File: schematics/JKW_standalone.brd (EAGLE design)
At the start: 159.4 x 80.7 mm, 241 parts, among them IC1 4093D, IC4 ATMEGA2560-16AU, Q1 BSS84, Q10 BSS84, Q11 BSS84, Q2 BSS84, Q3 BSS84, Q4 BSS84, Q5 BSS84, Q6 BSS84, Q7 BSS84, Q8 BSS84, Q9 BSS84, T1 Mouser: 771-2N7002BK215 , N-C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, T10 Mouser: 771-2N7002BK215 , N-C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, T11 Mouser: 771-2N7002BK215 , N-C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, T12 Mouser: 771-2N7002BK215 , N-C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, T13 Mouser: 771-2N7002BK215 , N-C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, T2 Mouser: 771-2N7002BK215 , N-C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, T3 Mouser: 771-2N7002BK215 , N-C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, T5 Mouser: 771-2N7002BK215 , N-C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, T6 Mouser: 771-2N7002BK215 , N-C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, T7 Mouser: 771-2N7002BK215 , N-C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, T8 Mouser: 771-2N7002BK215 , N-C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, T9 Mouser: 771-2N7002BK215 , N-C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

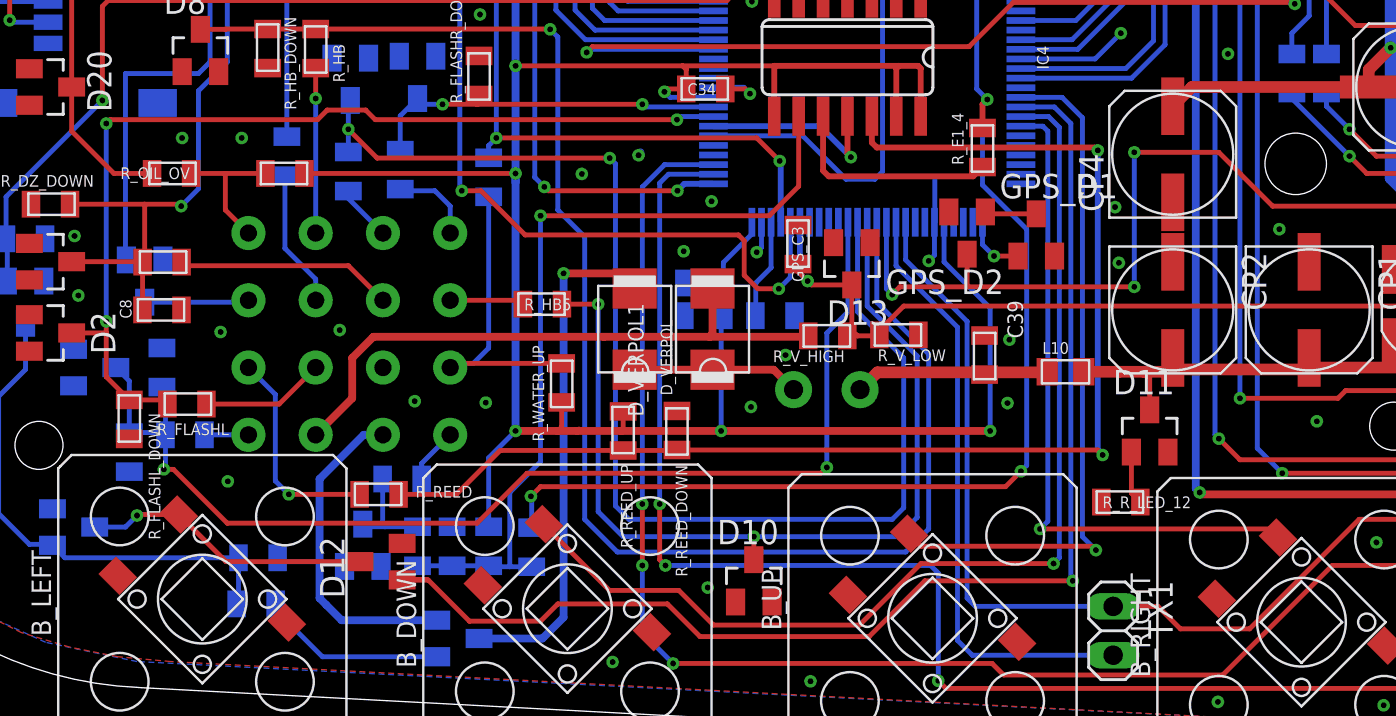
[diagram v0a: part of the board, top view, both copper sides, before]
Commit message: Readded Taster, changed pinning of taster, reduced resistor value, removed bat measurement connection (broke)
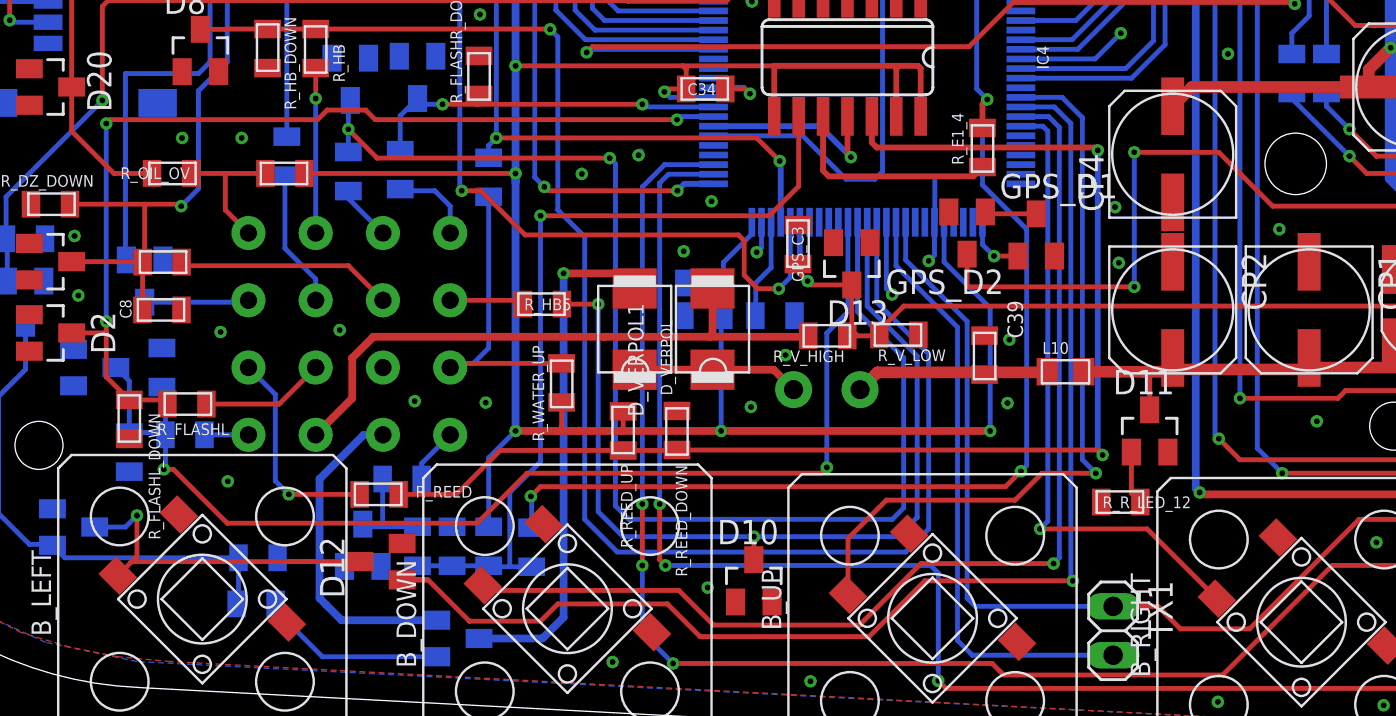
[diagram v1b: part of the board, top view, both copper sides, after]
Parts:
- R_L3: value 1k -> 10k
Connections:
- new net V_BAT: D15.C, GPS.VBACKUP, GPS_C2.1, GPS_D2.3
- net A11: no longer D15.C, GPS.VBACKUP, GPS_C2.1, GPS_D2.3
- net B_DOWN: now also B_DOWN.OUT; no longer B_DOWN.OUT1
- net B_LEFT: now also B_LEFT.OUT; no longer B_LEFT.OUT1
- net B_RIGHT: now also B_RIGHT.OUT; no longer B_RIGHT.OUT1
- net B_UP: now also B_UP.OUT; no longer B_UP.OUT1
- net GND: now also B_DOWN.IN2, B_LEFT.IN2, B_RIGHT.IN2, B_UP.IN2
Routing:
- net A11: track 111.8 -> 3.88 mm, vias 7 -> 1
- net V_BAT: track 0.00 -> 103.9 mm, vias 0 -> 6
- net B_UP: track 36.5 -> 39.7 mm
- net B_LEFT: track 15.1 -> 17.9 mm
- net B_RIGHT: track 35.0 -> 33.1 mm
- net B_DOWN: track 55.1 -> 56.9 mm

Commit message: Changed value of pullup to 15k
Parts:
- R_REED_DOWN: value 5k / n.b. (Reed / 5V Honda Signal) -> 5k / n.b. (12V Signal / 5V Signal)
- R_REED_UP: value n.b.(Honda Signal) / 5k (Reed) -> n.b.(Honda Signal) / 15k (Reed)
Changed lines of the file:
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@@
 <?xml version="1.0" encoding="utf-8"?>
 <!DOCTYPE eagle SYSTEM "eagle.dtd">
-<eagle version="6.2">
+<eagle version="6.4">
 <drawing>
 <settings>
@@
 </class>
 </classes>
-<designrules>
+<designrules name="default">
 <description language="de">DRC von Lutz
 Via´s bis 0.6mm mit Lötstoplack überzogen
@@
 <attribute name="NAME" x="133.1325" y="50.9975" size="0.6096" layer="26" rot="MR90"/>
 </element>
-<element name="R_REED_DOWN" library="RCLDT" package="0805" value="5k / n.b. (Reed / 5V Honda Signal)" x="38.6" y="17.525" smashed="yes" rot="R90">
+<element name="R_REED_DOWN" library="RCLDT" package="0805" value="5k / n.b. (12V Signal / 5V Signal)" x="38.6" y="17.525" smashed="yes" rot="R90">
 <attribute name="NAME" x="38.5325" y="15.7275" size="0.6096" layer="25" rot="R270"/>
 </element>
@@
 </element>
 <element name="D8" library="diode" package="SOT23" value="5.5V" x="13.8" y="37.3"/>
-<element name="R_REED_UP" library="RCLDT" package="0805" value="n.b.(Honda Signal) / 5k (Reed)" x="35.8" y="17.5" smashed="yes" rot="R270">
+<element name="R_REED_UP" library="RCLDT" package="0805" value="n.b.(Honda Signal) / 15k (Reed)" x="35.8" y="17.5" smashed="yes" rot="R270">
 <attribute name="NAME" x="35.6825" y="15.7525" size="0.6096" layer="25" rot="R270"/>
 <attribute name="VALUE" x="34.1825" y="20.1525" size="0.6096" layer="27" rot="R270"/>

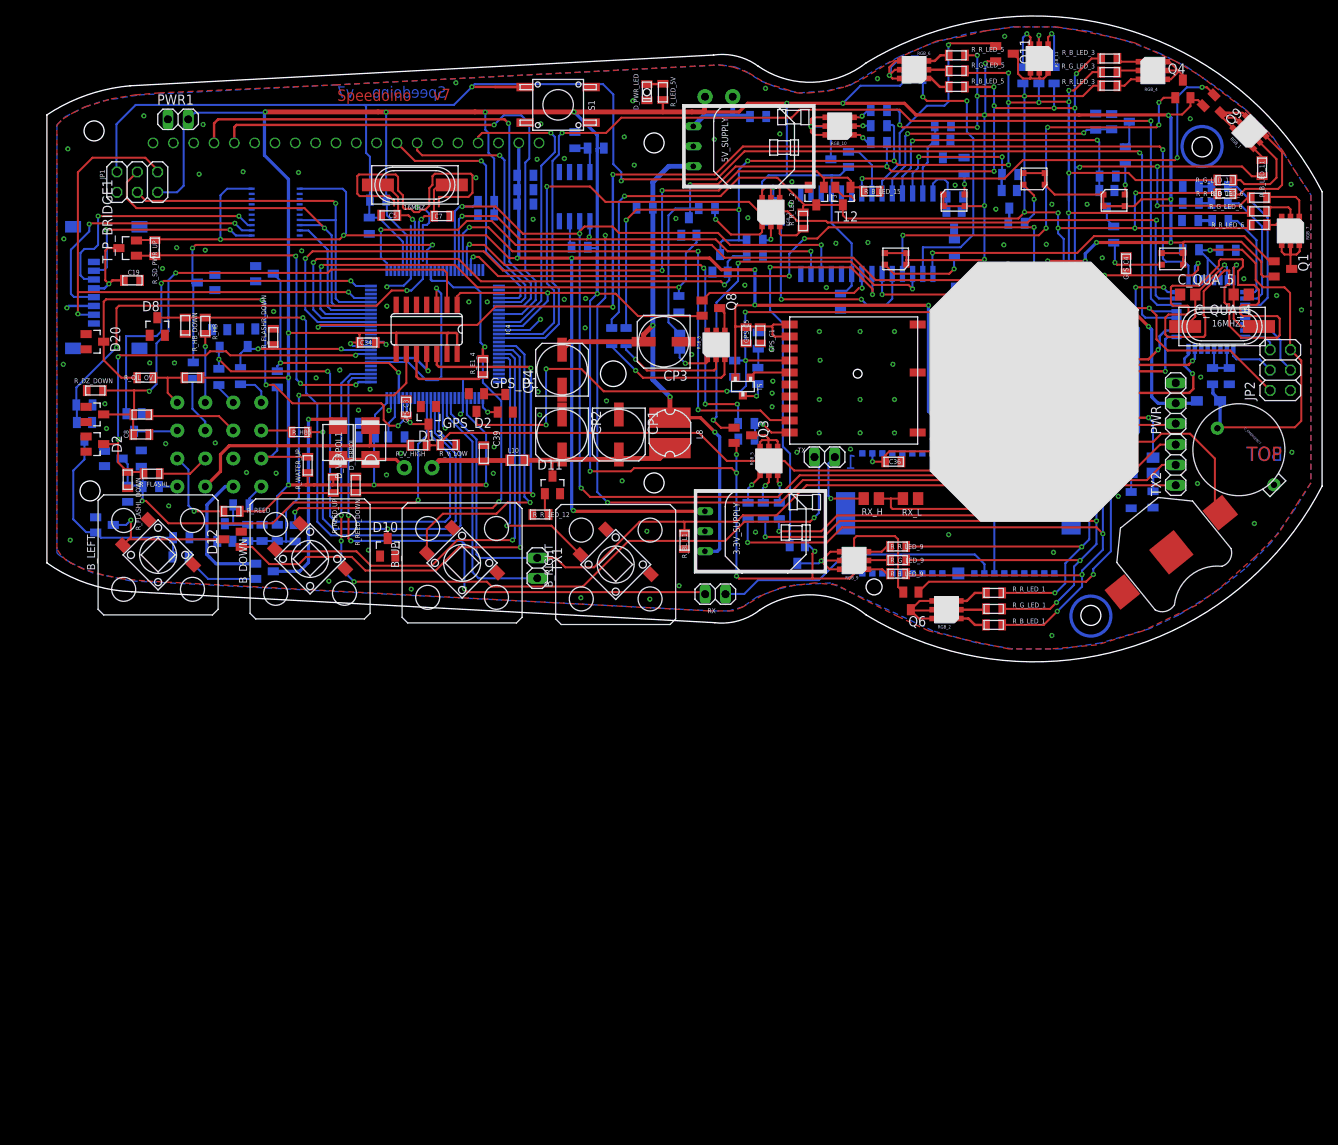
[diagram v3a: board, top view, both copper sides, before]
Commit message: Added CAN to PCB, Added OP to PCB, Modified drillsize of Connector Modified drillsize of Power Supply
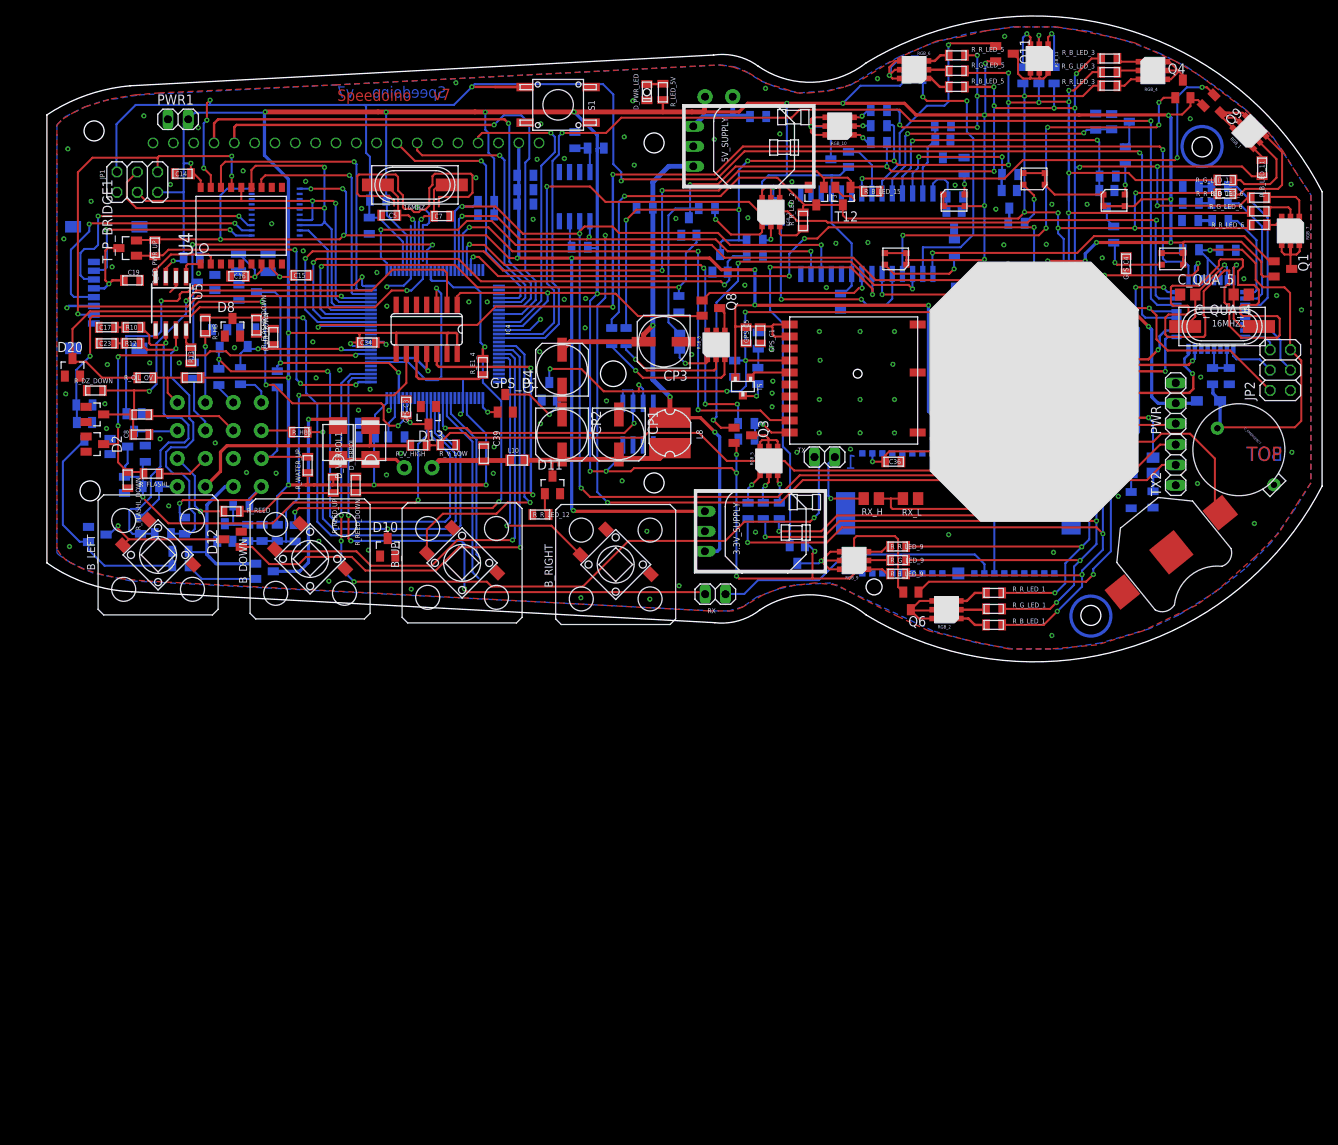
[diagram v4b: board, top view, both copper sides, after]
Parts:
- removed R_BL_L1: n.b., RCLDT:0805
- removed TX1: (no value), pinhead:1X02
- added C14, C22: 100n/20V, RCLDT:0805
- added C15, C16: 22pF, RCLDT:0805
- added C17, C23: 560p/20V, RCLDT:0805
- added IC2: LM1458D, linear:SO08
- added Q12: 16MHz, SparkFun:CRYSTAL-SMD-5X3
- added R1: 160, RCLDT:0805
- added R10, R12: 100, RCLDT:0805
- added R13: 4.7k, RCLDT:0805
- added R_E2_3, R_E2_4: n.b. / 0R, RCLDT:0805
- added U4: MCP2515, microchip_can:SO-18W
- added U5: MCP2551, skpang_lib:SO-08M
- moved D8 9.40 mm to (23.2, 37.2)
- moved GPS_D2 9.21 mm to (62.8, 29.2), flipped to the bottom, turned to 0 degrees
- moved R_HB_DOWN 8.90 mm to (26.2, 37.4)
- moved D20 4.25 mm to (3.20, 32.2), turned to 0 degrees
- moved D3 3.11 mm to (25.1, 41.6)
- moved R_DEAKT_DAUER_P 1.70 mm to (16.7, 9.20)
- moved D22 1.66 mm to (9.00, 22.3)
- moved D14 1.50 mm to (6.30, 11.3)
- moved R_E2_0 1.17 mm to (9.70, 17.5)
- moved R_DEAKT_DAUER_P2 1.10 mm to (16.7, 7.40)
- moved R_E2_2 0.78 mm to (12.3, 21.4)
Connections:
- new net CANH: R1.2, R12.2, R_E2_4.2, U5.7
- new net CANL: R1.1, R10.2, R_E2_3.1, U5.6
- new net CAN_RXD: U4.2, U5.4
- new net CAN_TXD: U4.1, U5.1
- new net N$112: R13.2, U5.8
- new net N$113: C15.1, Q12.3, U4.8
- new net N$114: C16.1, Q12.1, U4.7
- new net N$46: C17.2, R10.1
- new net N$89: C23.2, R12.1
- net A11: now also IC2.1, IC2.2
- net A12: no longer TX1.2
- net A13: no longer R_BL_L1.1, TX1.1, TX2.1
- net ARD_RES_OUT: now also U4.17
- net D10: now also U4.12
- net D11: now also U4.16
- net D50: now also U4.15
- net D51: now also U4.14
- net D52: now also U4.13
- net GND: now also C14.1, C15.2, C16.2, C17.1, C22.1, C23.1, IC2.4, R13.1, U4.9, U5.2; no longer R_BL_L1.2
- net N$42: now also R_E2_4.1
- net N$43: now also R_E2_3.2
- net VDD: now also C14.2, C22.2, IC2.8, U4.18, U5.3
- net V_BAT: now also IC2.3
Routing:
- net A13: track 114.6 -> 21.5 mm
- net CANL: track 0.00 -> 40.3 mm, vias 0 -> 1
- net CANH: track 0.00 -> 39.0 mm, vias 0 -> 1
- net D11: track 0.00 -> 37.4 mm, vias 0 -> 1
- net A11: track 3.88 -> 35.2 mm, vias 1 -> 2
- net D10: track 0.00 -> 29.5 mm, vias 0 -> 1
- net VDD: track 722.2 -> 743.7 mm, vias 31 -> 34
- net D52: track 48.1 -> 66.3 mm, vias 1 -> 2
- net D50: track 68.3 -> 82.8 mm, vias 2 -> 4
- net V_BAT: track 103.9 -> 90.4 mm
- net N$42: track 2.91 -> 16.1 mm, vias 0 -> 1
- net ARD_RES_OUT: track 206.5 -> 218.7 mm, vias 3 -> 6
- net CAN_RXD: track 0.00 -> 9.57 mm
- net A12: track 31.5 -> 24.2 mm
- net N$114: track 0.00 -> 6.88 mm, vias 0 -> 1
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
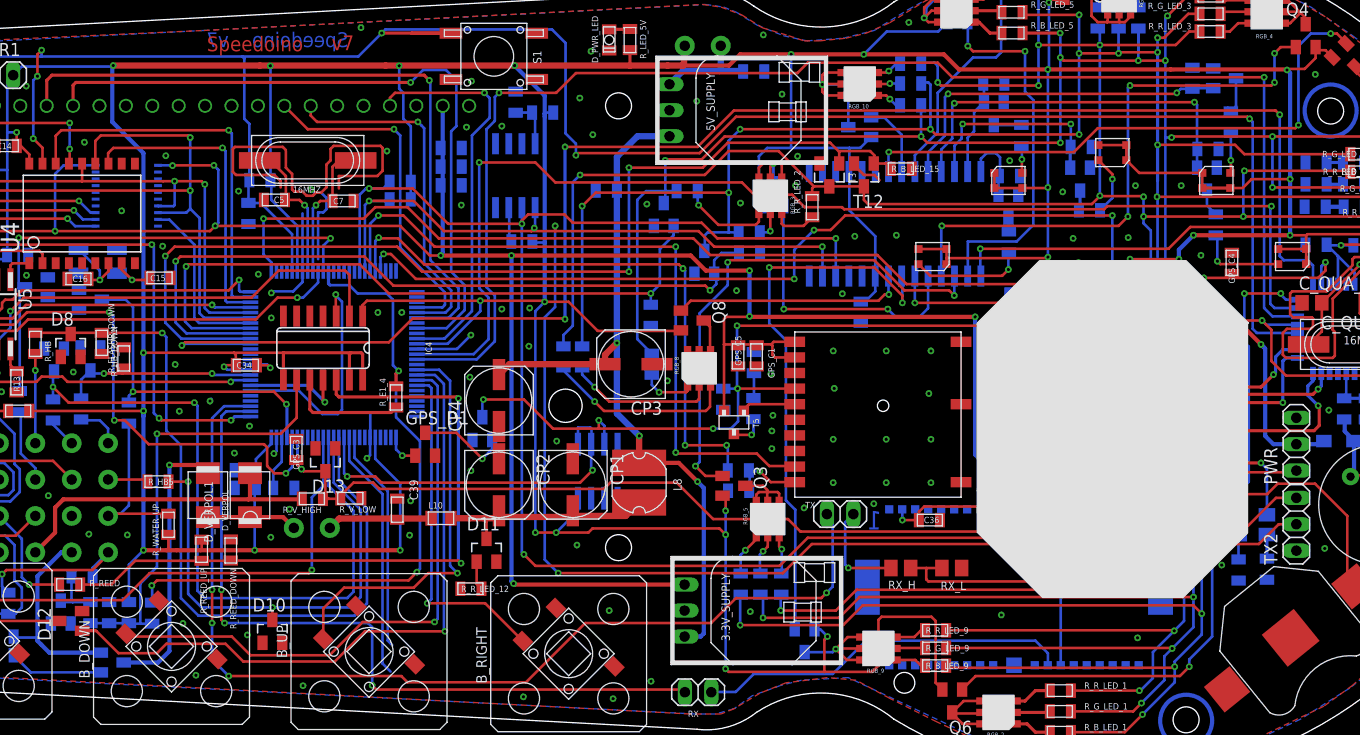
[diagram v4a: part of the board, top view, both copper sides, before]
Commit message: Added CAN to PCB
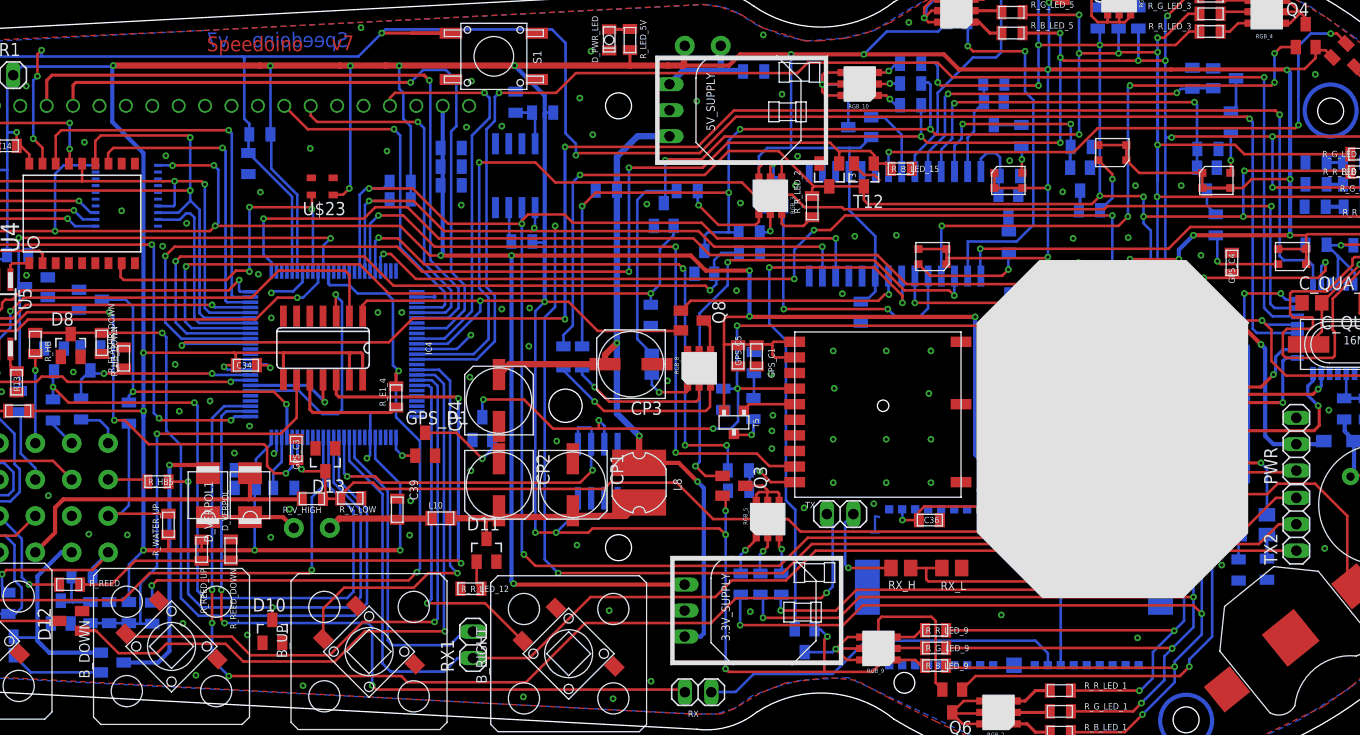
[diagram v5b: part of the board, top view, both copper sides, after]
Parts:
- removed 16MHZ: 16Mhz, XT:XT-HC49S-SMD
- removed C15, C16, C5, C7: 22pF, RCLDT:0805
- removed Q12: 16MHz, SparkFun:CRYSTAL-SMD-5X3
- added RX1: (no value), pinhead:1X02
- added U$23: ASE, crystal:ASE
- moved C35 4.80 mm to (40.3, 54.7)
- moved R_RES_UP 4.40 mm to (41.4, 57.5)
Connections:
- removed net N$113: C15.1, Q12.3, U4.8
- removed net N$114: C16.1, Q12.1, U4.7
- removed net N$35: 16MHZ.2, C5.1, IC4.33
- removed net N$36: 16MHZ.1, C7.1, IC4.34
- removed net N$48: IC4.52
- new net 16MHZ: IC4.34, U$23.3, U4.8
- new net N$115: IC4.51
- net A12: now also RX1.1, TX2.1
- net A13: now also RX1.2
- net GND: now also IC4.52, U$23.2; no longer C15.2, C16.2, C5.2, C7.2, IC4.51
- net VDD: now also U$23.4
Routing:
- net A12: track 24.2 -> 116.1 mm
- net GND: track 150.6 -> 100.8 mm, vias 127 -> 128
- net 16MHZ: track 0.00 -> 34.0 mm, vias 0 -> 3
- net VDD: track 743.7 -> 758.3 mm, vias 34 -> 36
- net N$35: track 14.1 -> 0.00 mm, vias 1 -> 0
- net N$36: track 14.1 -> 0.00 mm, vias 1 -> 0
- net A13: track 21.5 -> 29.8 mm
- net N$114: track 6.88 -> 0.00 mm, vias 1 -> 0
- net N$113: track 5.59 -> 0.00 mm, vias 1 -> 0
- net D53: track 17.2 -> 19.2 mm
- net ARD_RES_OUT: track 218.7 -> 218.0 mm
